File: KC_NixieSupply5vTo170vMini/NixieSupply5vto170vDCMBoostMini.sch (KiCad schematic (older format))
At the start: 40 parts, among them J1 Screw_Terminal_01x04, J2 CONN_01X01, J3 CONN_01X01, J4 CONN_01X01, J5 CONN_01X01, P1 USB_OTG, Q1 FDS2672CT, Q26 MMBTA42, U1 UCC3803

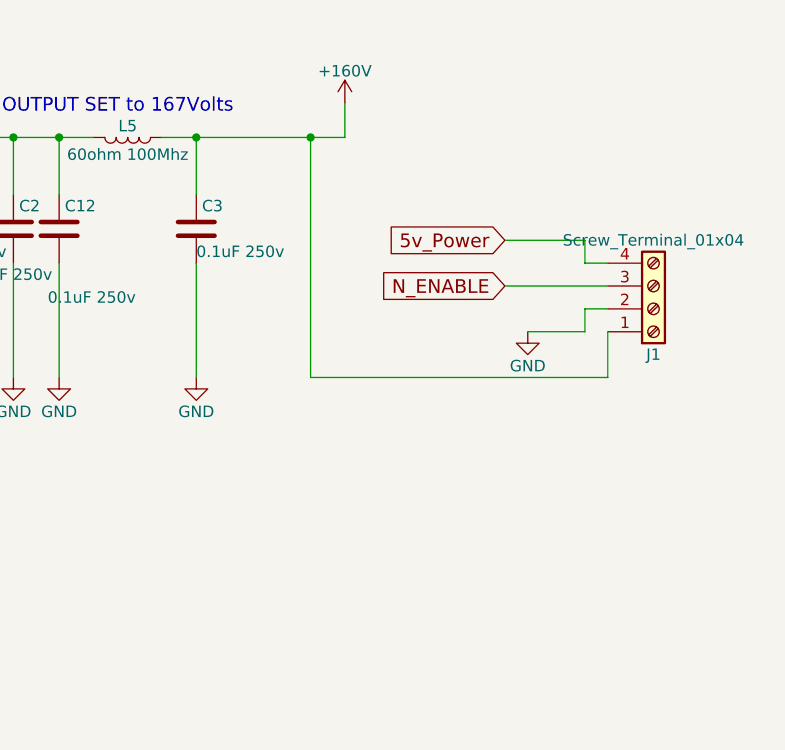
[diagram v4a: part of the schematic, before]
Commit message: Rev 3 of the Mini Nixie Tube Power supply schematic and layout. Changed the output connector to have 1.25mm spacing with nearest conductor
Moved traces around to allow forn two output connectors.    Changed
the size of the 47uF 16v capacitor to a 1210 package.
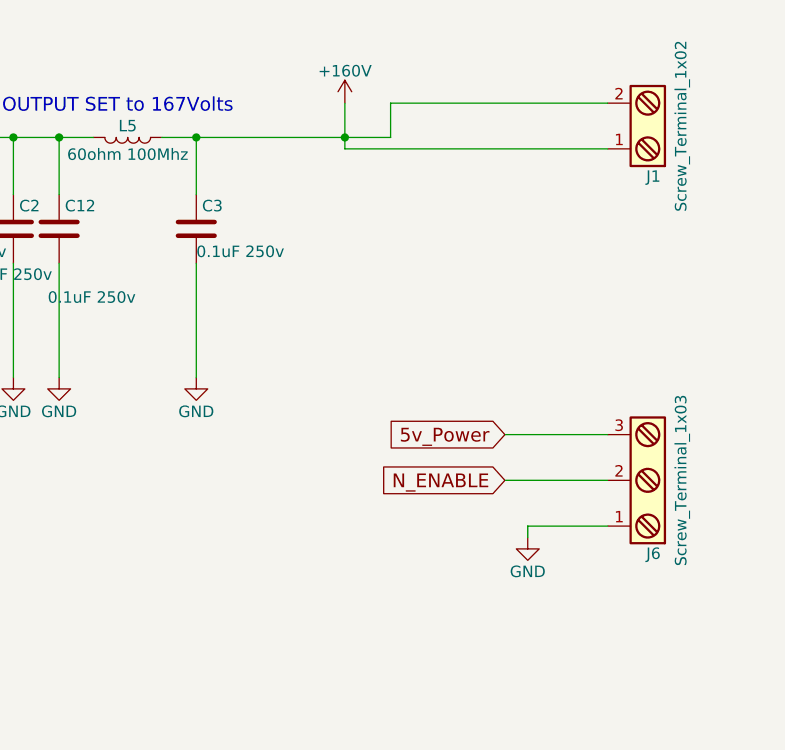
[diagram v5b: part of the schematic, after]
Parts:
- removed J1: Screw_Terminal_01x04, TerminalBlock_Phoenix:TerminalBlock_Phoenix_MPT-2.54mm_4pol, symbol Screw_Terminal_01x04
- added J1: Screw_Terminal_1x02, TerminalBlock_Phoenix:TerminalBlock_Phoenix_MPT-2.54mm_2pol, symbol Screw_Terminal_1x02
- added J6: Screw_Terminal_1x03, TerminalBlock_Phoenix:TerminalBlock_Phoenix_MPT-2.54mm_3pol, symbol Screw_Terminal_1x03
- C14: footprint Capacitors_SMD:C_1206 -> Capacitors_SMD:C_1210; MPN C3216JB1C476M160AB -> EMK325BJ476MM-P
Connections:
- net +160V: now also J1.1, J1.2
- net 5v_Power: now also J6.3
- net GND: now also J6.1
- net N_ENABLE: now also J6.2

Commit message: The NewOrigin Zip file was used for the PCBWAY order This BOM was used for the PCBway order Updated the files to Rev 5 of Kicad
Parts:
- C1, C14, C15, C16, C2, C6, C7, C9: symbol C -> Device:C
- C10, C18: symbol C -> Device:C; MAN (none) -> KEMET; MPN (none) -> C0805C104K3RACTU
- C11: symbol C -> Device:C; MAN (none) -> KEMET; MPN (none) -> C0805C102M5RACTU
- C12, C3: symbol C -> Device:C; MAN (none) -> TDK; MPN (none) -> CGA4J3X7T2E104M125AE
- C5: symbol C -> Device:C; MAN (none) -> KEMET; MPN (none) -> C0805C221M5RACTU
- D1: symbol D -> Device:D
- D2: symbol D_Schottky -> Device:D_Schottky
- J1: symbol Screw_Terminal_1x02 -> NixieSupply5vto170vDCMBoostMini-rescue:Screw_Terminal_1x02; MAN (none) -> Phoenix
- J2, J3, J4, J5: symbol Conn_01x01 -> Connector_Generic:Conn_01x01
- J6: symbol Screw_Terminal_1x03 -> NixieSupply5vto170vDCMBoostMini-rescue:Screw_Terminal_1x03; MAN (none) -> Phoenix
- L2: symbol L -> NixieSupply5vto170vDCMBoostMini-rescue:L; MPN BKP2125HS600-T -> BKP2125HS600-T
- L3: symbol L -> NixieSupply5vto170vDCMBoostMini-rescue:L; MAN (none) -> Wurth
- L5: symbol L -> NixieSupply5vto170vDCMBoostMini-rescue:L; MPN (none) -> BKP2125HS600-T
- P1: symbol USB_OTG -> NixieSupply5vto170vDCMBoostMini-rescue:USB_OTG; MAN (none) -> Wurth
- Q1: symbol FDMS86255ET150 -> NixieSupply5vto170vDCMBoostMini-rescue:FDMS86255ET150; MAN (none) -> On-Semi
- Q26: symbol MMBT3904 -> Transistor_BJT:MMBT3904
- R1, R8: symbol R -> Device:R; MAN (none) -> Yageo; MPN (none) -> RC0805FR-071KL
- R10: symbol R -> Device:R; MAN (none) -> Panasonic
- R12: symbol R -> Device:R; MAN (none) -> Yageo; MPN (none) -> RC0805FR-074K12L
- R15: symbol R -> Device:R; MAN (none) -> Yageo; MPN (none) -> RC0805FR-07634KL
- R16: symbol R -> Device:R; MAN (none) -> Yageo; MPN (none) -> RC0805FR-077K68L
- R2: symbol R -> Device:R; MAN (none) -> Yageo; MPN (none) -> RC0805FR-0760K4L
- R3: symbol R -> Device:R
- R4, R9: symbol R -> Device:R; MAN (none) -> Yageo; MPN (none) -> RC0805FR-07100KL
- R5: symbol R -> Device:R; MAN (none) -> Yageo; MPN (none) -> RC0805FR-070RL
- R7: symbol R -> Device:R; MAN (none) -> Yageo; MPN (none) -> RC0805FR-072KL
- U1: symbol AAC243 -> NixieSupply5vto170vDCMBoostMini-rescue:AAC243; MAN (none) -> TI
